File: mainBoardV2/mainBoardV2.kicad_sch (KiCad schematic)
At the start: 24 parts, among them J1 USB4125-GF-A_REVA2, U3 MCP73871-2AAI_ML, U4 MPU6050_Module, U5 TPS61023DRLT

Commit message: 3.17.26.C1
inserted a true NTC thermistor, set to operate from 0 to 50C. Added two Vout vias for use with the board outside of the connection to the IMU. Add through holes to feed jst wires or the NTC bead through. Added notes to schematic, and included ESP32 devkit, 2 cams on the schematic (but not board)
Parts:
- added R3: 1.5k, Resistor_SMD:R_0805_2012Metric_Pad1.20x1.40mm_HandSolder, symbol Device:R
- added R4: 70k, Resistor_SMD:R_0805_2012Metric_Pad1.20x1.40mm_HandSolder, symbol Device:R
- added U1: ESP32-DEVKITC-32E, ESP32-DEVKITC-32E:MODULE_ESP32-DEVKITC-32E, symbol ESP32-DEVKITC-32E:ESP32-DEVKITC-32E
- added U2, U8: ESP32-CAM, ESP32-CAM:ESP32-CAM, symbol ESP32-CAM:ESP32-CAM
- R13: footprint Resistor_SMD:R_0805_2012Metric_Pad1.20x1.40mm_HandSolder -> TPS61023DRLT:103AT-11_NTC_throughole
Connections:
- net +5V: now also U1.J2_19 (EXT_5V), U2.9 (5V), U8.9 (5V)
- net GND: now also J1.S1 (SHIELD), J1.S2 (SHIELD), J1.S3 (SHIELD), J1.S4 (SHIELD), U4.GND, R4.2, U1.J2_14 (GND_J2_14), U2.10 (GND@3), U8.10 (GND@3)
- net Therm: now also R3.1; no longer R13.2
- new net: R13.2, R3.2, R4.1
- no-connect marks 2 -> 1
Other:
- note added: "5V to devkit, two cams, and IMU will come from connection to the booster/charging circuit."
- note added: "ON/OFF will be between VBatt+ and input Capacitor C1"
- note added: "R13 is the thermistor. 1.5K in series with it, and 70K parallel to it, means an operating temp range of 0C to 50C before charge circuit turns off."
- note removed: "ON/OFF Here"
- moved on the sheet: C5, R13, U6

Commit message: 3.17.26.C2
Added tantalum capacitors to output of boost converter. Have created gerber and drill files after running DRC check until only thing left were some clearance warnings. manufacturer can handle.
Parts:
- C2, C3: footprint Capacitor_SMD:C_0805_2012Metric_Pad1.18x1.45mm_HandSolder -> Capacitor_Tantalum_SMD:CP_EIA-6032-15_Kemet-U_HandSolder
- R10: value 470k -> 300
- R9: value 470k -> 160
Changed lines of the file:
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@@
 			)
 		)
-		(property "Value" "470k"
+		(property "Value" "300"
 			(at 99.06 50.8 90)
 			(effects
@@
 			)
 		)
-		(property "Footprint" "Capacitor_SMD:C_0805_2012Metric_Pad1.18x1.45mm_HandSolder"
+		(property "Footprint" "Capacitor_Tantalum_SMD:CP_EIA-6032-15_Kemet-U_HandSolder"
 			(at 256.2352 115.57 0)
 			(effects
@@
 			)
 		)
-		(property "Footprint" "Capacitor_SMD:C_0805_2012Metric_Pad1.18x1.45mm_HandSolder"
+		(property "Footprint" "Capacitor_Tantalum_SMD:CP_EIA-6032-15_Kemet-U_HandSolder"
 			(at 267.6652 115.57 0)
 			(effects
@@
 			)
 		)
-		(property "Value" "470k"
+		(property "Value" "160"
 			(at 99.314 43.18 90)
 			(effects

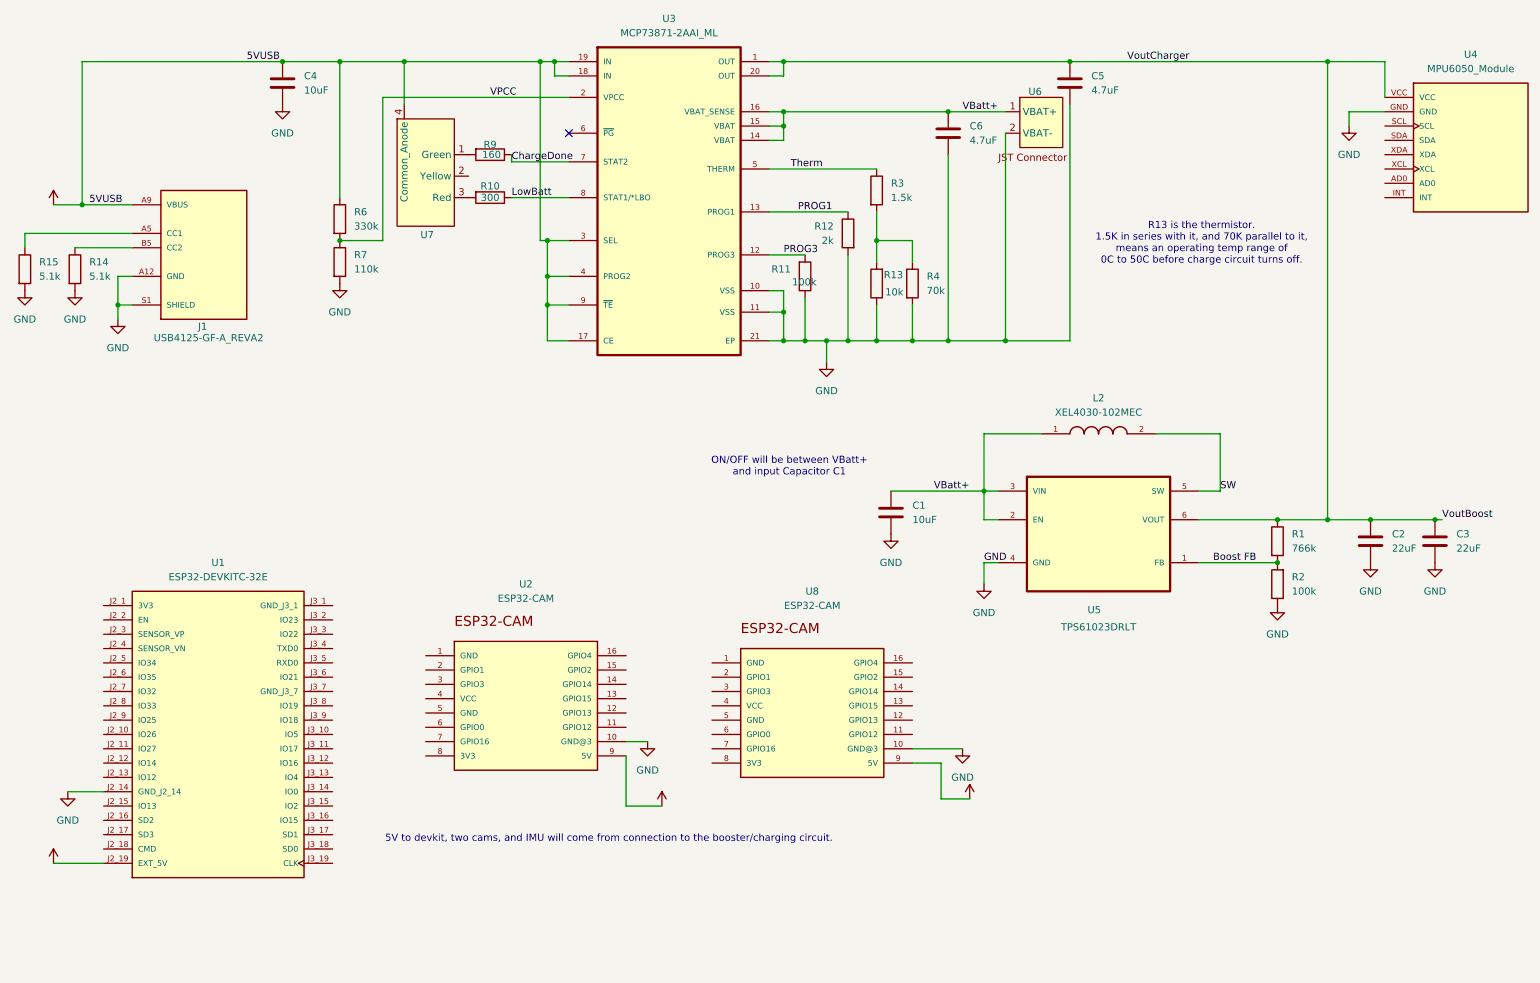
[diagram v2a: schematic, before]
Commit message: Closing project on laptop.
Not closing this commit first before opening project on another device created a branch
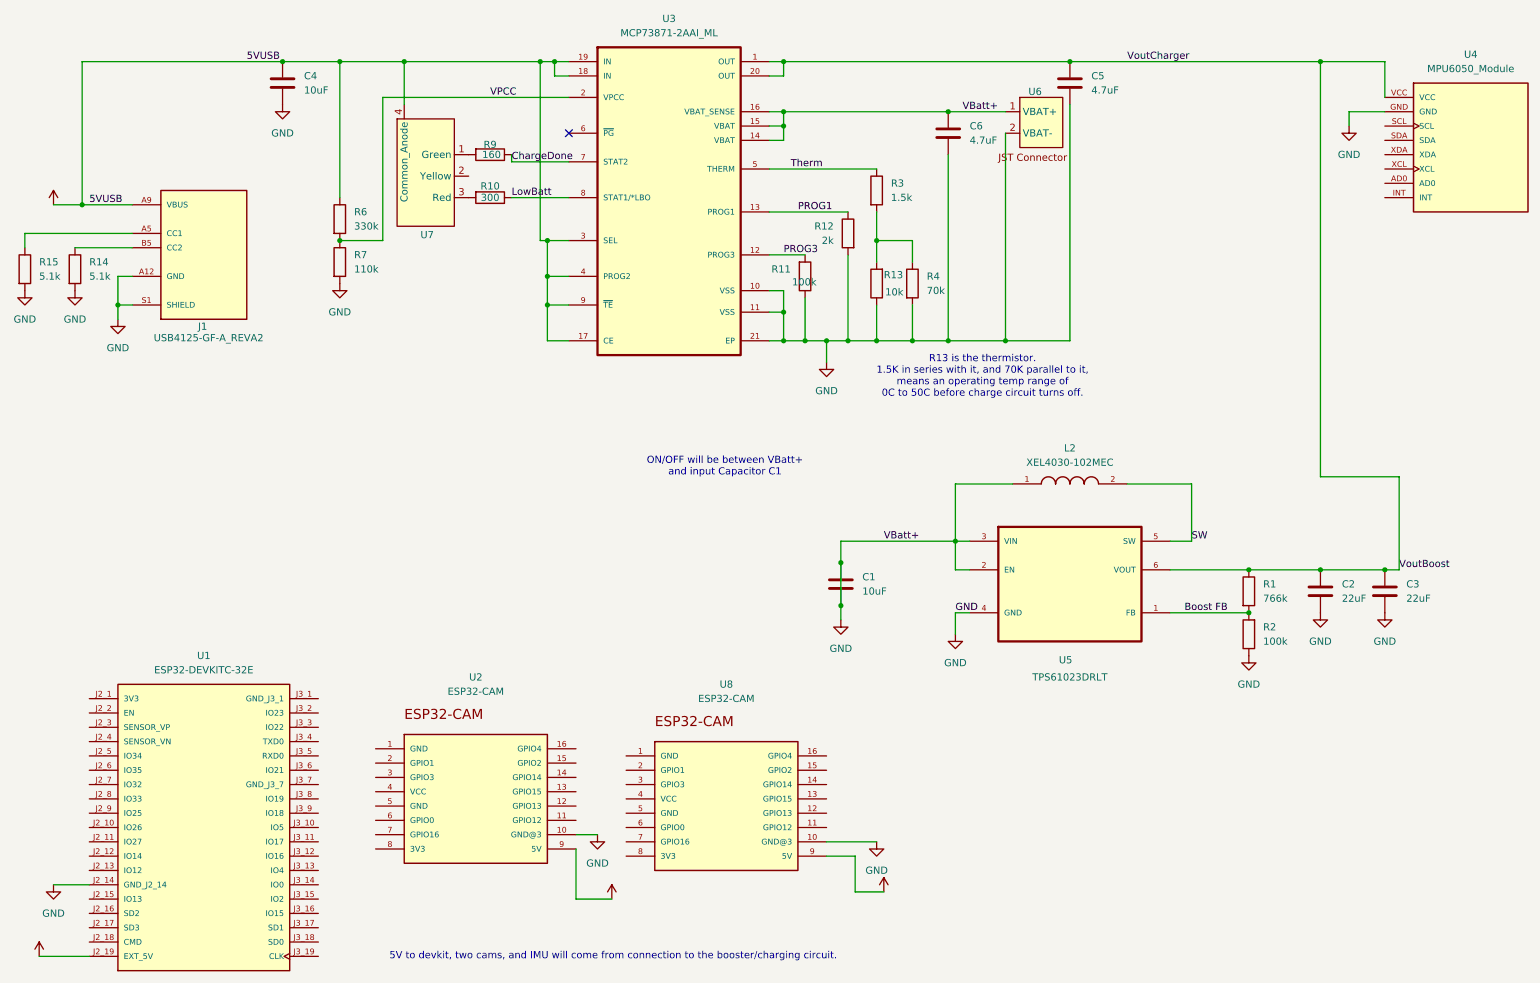
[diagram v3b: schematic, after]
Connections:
- net VBatt+ is gone; now on net GND: C1.1, C6.1, L2.1, U3.14 (VBAT), U3.15 (VBAT), U3.16 (VBAT_SENSE), U5.2 (EN), U5.3 (VIN), U6.1 (VBAT+)
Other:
- moved on the sheet: C1, C2, C3, L2, R1, R2, U1, U2, U5, U8
